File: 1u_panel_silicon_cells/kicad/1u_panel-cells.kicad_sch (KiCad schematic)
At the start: 25 parts, among them U13 LTC4411, U14 LTC4411, U15 LTC4411, U16 LTC4411, U5 LTC4411, U6 LTC4411, U8 LTC4411, U9 LTC4411

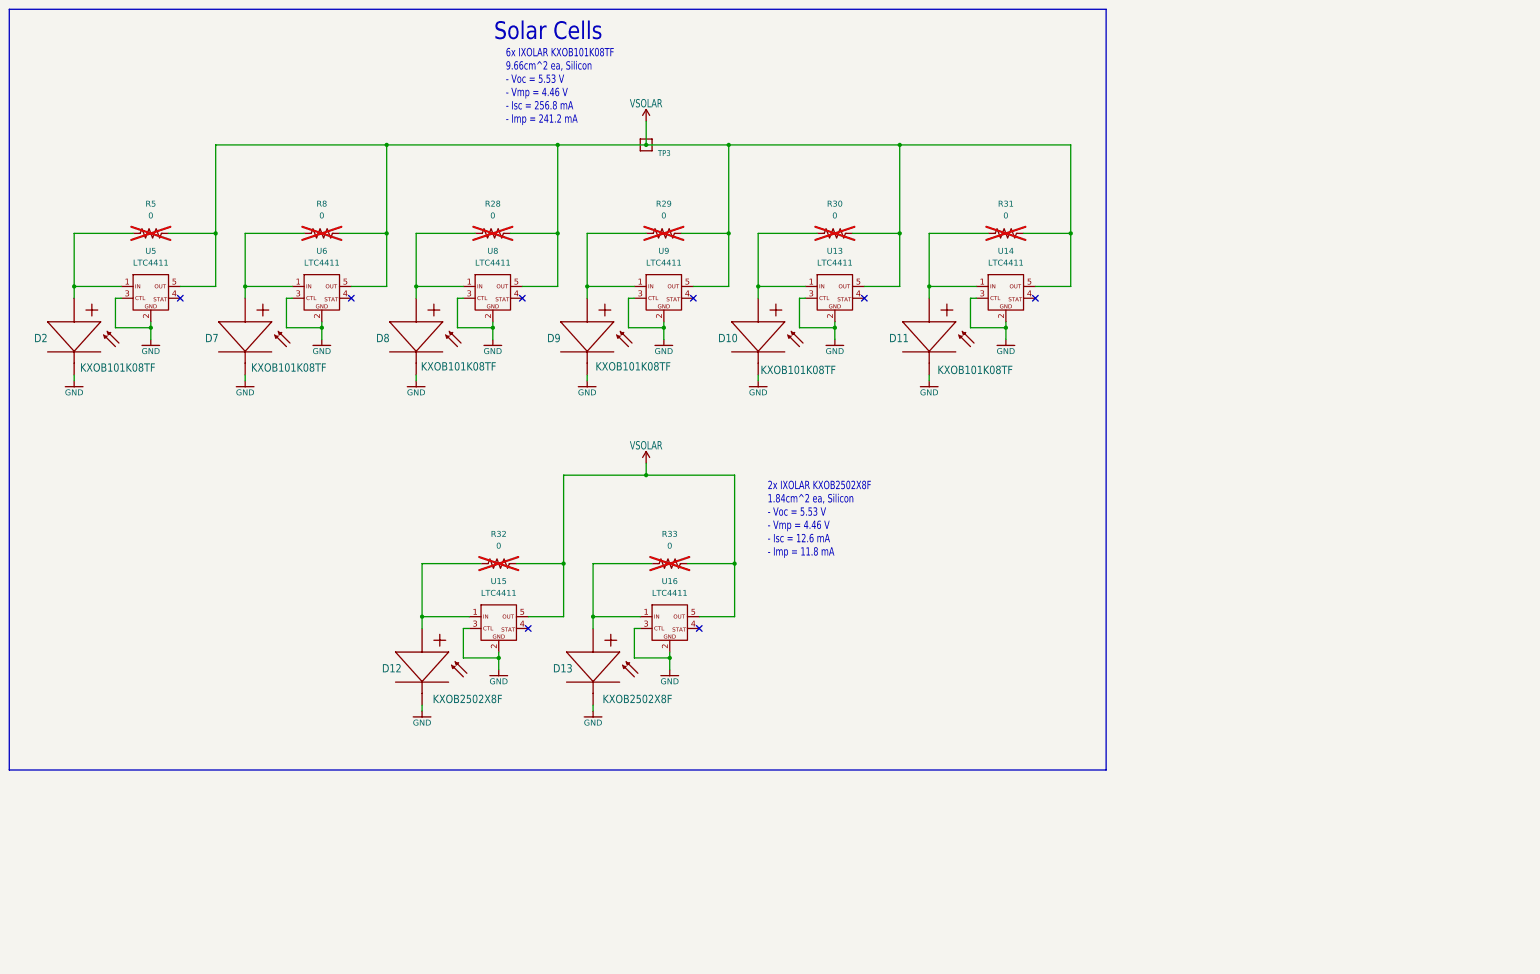
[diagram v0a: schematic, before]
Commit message: fixed board outline, title blocks
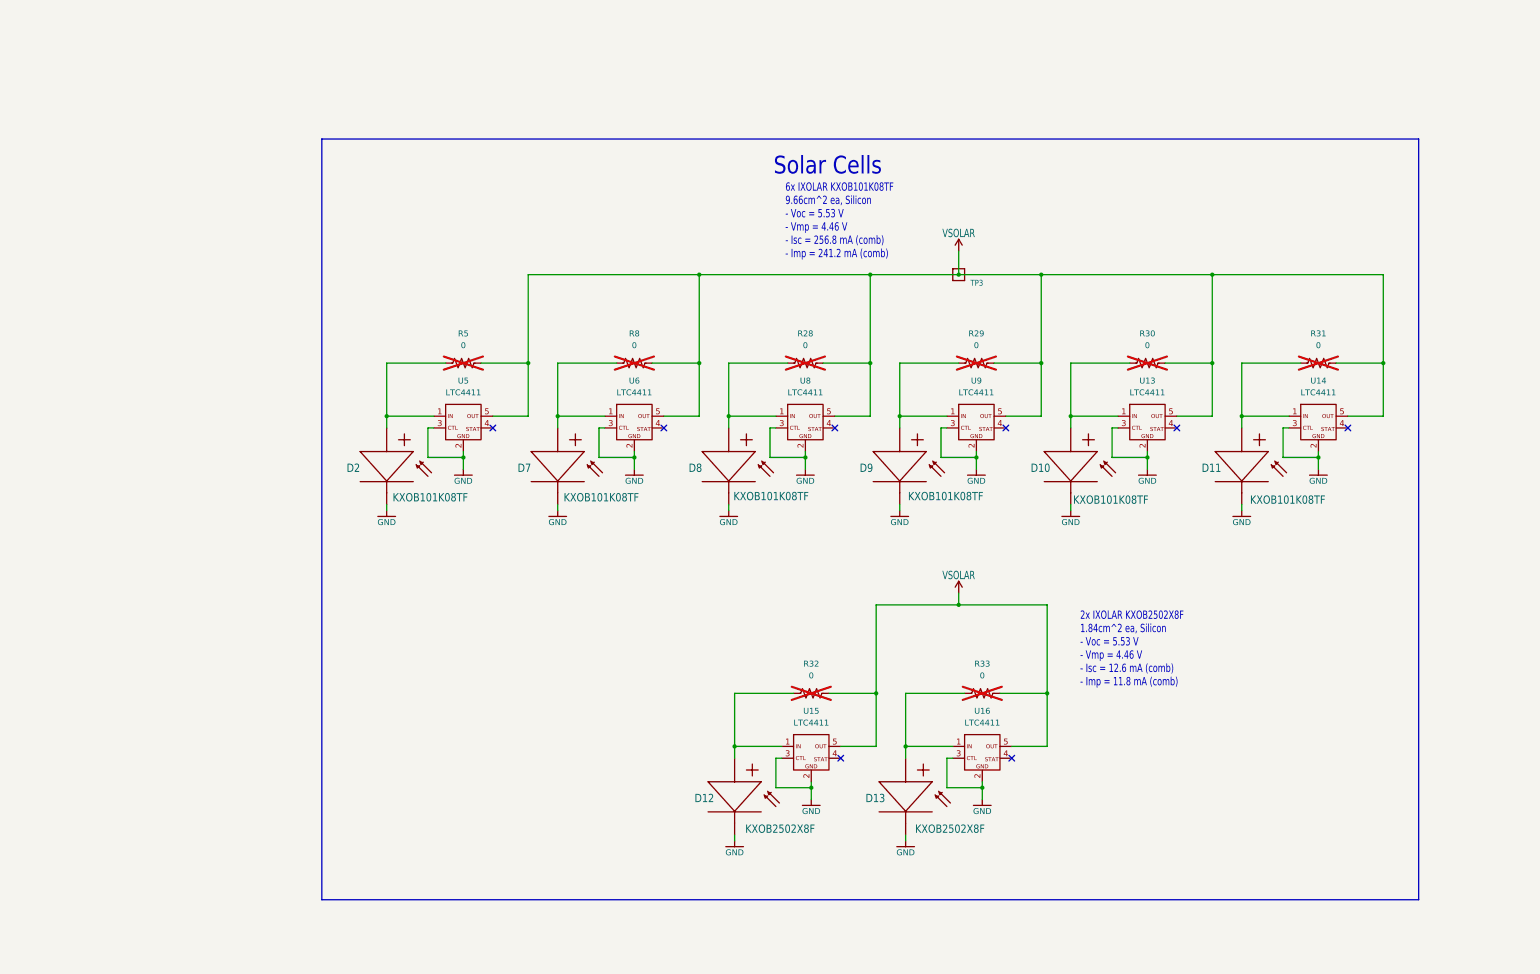
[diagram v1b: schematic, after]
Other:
- note added: "2x IXOLAR KXOB2502X8F 1.84cm^2 ea, Silicon - Voc = 5.53 V - Vmp = 4.46 V - Isc = 12.6 mA (comb) - Imp = 11.8 mA (comb)"
- note added: "6x IXOLAR KXOB101K08TF 9.66cm^2 ea, Silicon - Voc = 5.53 V - Vmp = 4.46 V - Isc = 256.8 mA (comb) - Imp = 241.2 mA (comb)"
- note removed: "2x IXOLAR KXOB2502X8F 1.84cm^2 ea, Silicon - Voc = 5.53 V - Vmp = 4.46 V - Isc = 12.6 mA - Imp = 11.8 mA"
- note removed: "6x IXOLAR KXOB101K08TF 9.66cm^2 ea, Silicon - Voc = 5.53 V - Vmp = 4.46 V - Isc = 256.8 mA - Imp = 241.2 mA"
- title: OreSat Solar Module (for Frame 2.0) -> OreSat Silicon Solar Module (for Frame 2.0)
- moved on the sheet: D10, D11, D12, D13, D2, D7, D8, D9, R28, R29, R30, R31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

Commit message: commiting silicon solar panel before moving programming header
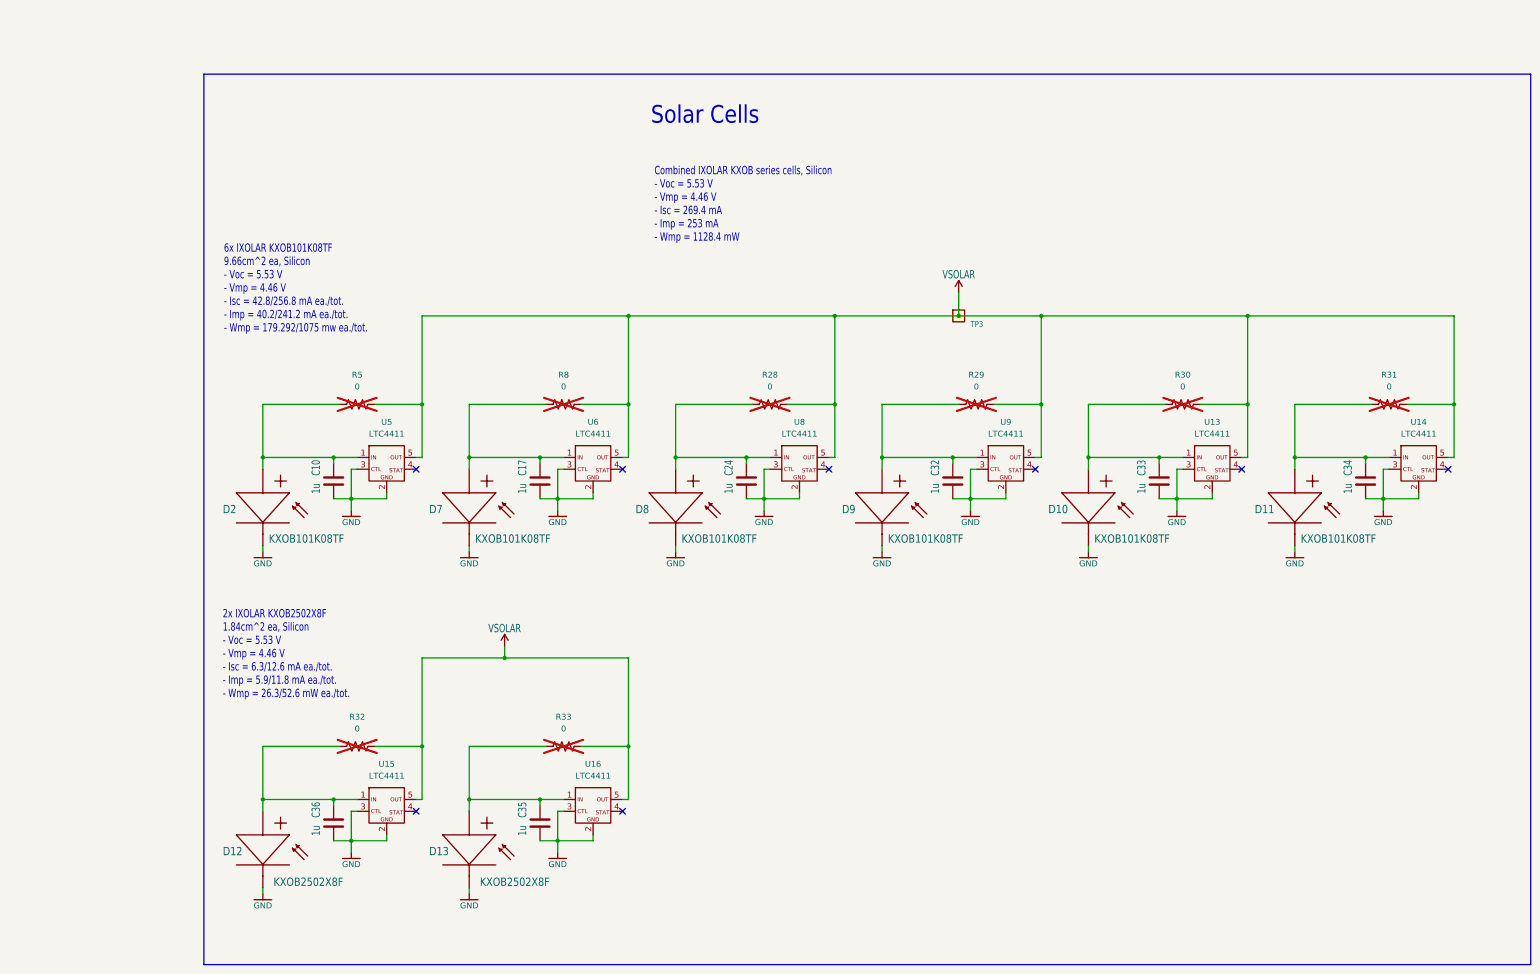
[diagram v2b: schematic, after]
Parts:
- added C10, C17, C24, C32, C33, C34, C35, C36: 1u, oresat-passives:0603-C-NOSILK, symbol Device:C
- D10, D11, D2, D7, D8, D9: DIS (none) -> Digi-Key; DPN (none) -> 2994-KXOB101K08TF-TR-ND; MFR (none) -> Anysolar; MPN (none) -> KXOB101K08TF-TR
- D12, D13: DIS (none) -> Digi-Key; DPN (none) -> KXOB25-02X8FTR-ND; MFR (none) -> Anysolar; MPN (none) -> KXOB25-02X8F-TR
- R28, R29, R30, R31, R32, R33, R5, R8: footprint 1u_panel:.0603-C-NOSILK -> oresat-passives:0603-C-NOSILK
- TP3: footprint 1u_panel:1X01 -> oresat-misc:TestPoint-0.75mm-th; symbol 1u_panel-eagle-import:TEST-POINT-LARGE-SQUARE -> oresat-misc:Test-Point-0.75mm-th; now left out of the parts list
- U13, U14, U15, U16, U5, U6, U8, U9: DIS (none) -> Digi-Key; DPN (none) -> 505-LTC4411ES5#TRMPBFTR-ND; MFR (none) -> Analog Devices; MPN (none) -> LTC4411ES5#TRMPBF
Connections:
- net GND: now also C10.2, C17.2, C24.2, C32.2, C33.2, C34.2, C35.2, C36.2
- net at D11.POS1 (A1), R31.1, U14.1: now also C34.1
- net at D9.POS1 (A1), R29.1, U9.1: now also C32.1
- net at D7.POS1 (A1), R8.1, U6.1: now also C17.1
- net at D8.POS1 (A1), R28.1, U8.1: now also C24.1
- net at D12.POS1 (A1), R32.1, U15.1: now also C36.1
- net at D2.POS1 (A1), R5.1, U5.1: now also C10.1
- net at D10.POS1 (A1), R30.1, U13.1: now also C33.1
- net at D13.POS1 (A1), R33.1, U16.1: now also C35.1
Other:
- note added: "2x IXOLAR KXOB2502X8F 1.84cm^2 ea, Silicon - Voc = 5.53 V - Vmp = 4.46 V - Isc = 6.3/12.6 mA ea./tot. - Imp = 5.9/11.8 mA ea./tot. - Wmp = 26.3/52.6 mW ea./tot."
- note added: "6x IXOLAR KXOB101K08TF 9.66cm^2 ea, Silicon - Voc = 5.53 V - Vmp = 4.46 V - Isc = 42.8/256.8 mA ea./tot. - Imp = 40.2/241.2 mA ea./tot. - Wmp = 179.292/1075 mw ea./tot."
- note added: "Combined IXOLAR KXOB series cells, Silicon - Voc = 5.53 V - Vmp = 4.46 V - Isc = 269.4 mA - Imp = 253 mA - Wmp = 1128.4 mW"
- note removed: "2x IXOLAR KXOB2502X8F 1.84cm^2 ea, Silicon - Voc = 5.53 V - Vmp = 4.46 V - Isc = 12.6 mA (comb) - Imp = 11.8 mA (comb)"
- note removed: "6x IXOLAR KXOB101K08TF 9.66cm^2 ea, Silicon - Voc = 5.53 V - Vmp = 4.46 V - Isc = 256.8 mA (comb) - Imp = 241.2 mA (comb)"
- moved on the sheet: D2, R5, U5

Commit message: Polish on Jack's final design. Swapped out rectangles for zones on multiple layers, cleaned up a lot of small layout bits, fixed some mechanical crashes with screw heads, fixed up the silk screen, and added 3D models.
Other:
- title: OreSat Silicon Solar Module (for Frame 2.0) -> OreSat Solar Module - Silicon Cells
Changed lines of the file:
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@@
 	(generator "eeschema")
 	(generator_version "8.0")
-	(paper "User" 431.8 279.4)
+	(paper "USLedger")
 	(title_block
-		(title "OreSat Silicon Solar Module (for Frame 2.0)")
-		(date "2024-08-18")
+		(title "OreSat Solar Module - Silicon Cells")
+		(date "2024-09-22")
 		(rev "1.0")
 	)

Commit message: updated part numbers for all components on silicon module to be flight-ready hardware PNs, pulled from CFC mfr series'
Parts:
- C10, C17, C24, C32, C33, C34, C35, C36: DPN 1276-1946-2-ND -> 587-3473-1-ND; Distributor (none) -> Digi-Key; MFR Samsung -> Taiyo Yuden; MPN CL10B105KP8NNNC -> TMK107BJ105KAHT
- D10, D11, D12, D13, D2, D7, D8, D9, U13, U14, U15, U16, U5, U6, U8, U9: Distributor (none) -> Digi-Key
- R28, R29, R30, R31, R32, R33, R5, R8: DPN (none) -> P0.0GTR-ND; Distributor (none) -> Digi-Key; MFR (none) -> Panasonic; MPN (none) -> ERJ-3GEY0R00V
